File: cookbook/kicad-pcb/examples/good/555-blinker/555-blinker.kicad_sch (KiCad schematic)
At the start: 8 parts, among them J1 Conn_01x02, U1 NE555

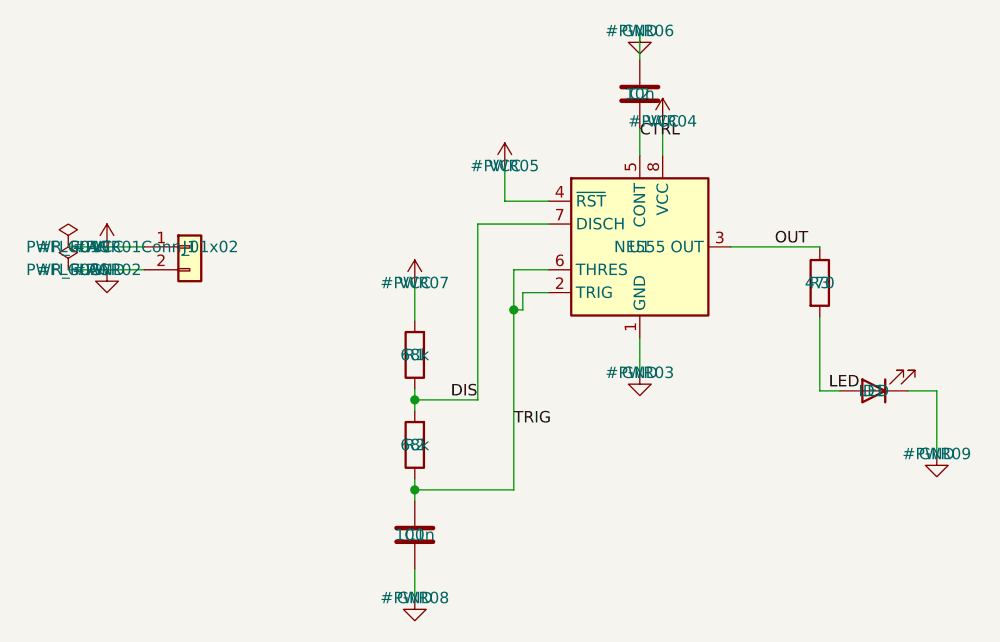
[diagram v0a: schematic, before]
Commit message: fix(cookbook/kicad-pcb): place schematic on 50-mil grid
The generator emitted pins and wire ends at arbitrary mm positions, so
ERC reported 51 endpoint_off_grid warnings. Move all coordinates to
integer 50-mil grid units (1.27 mm); symbol pin offsets are already
exact grid multiples so every endpoint lands on grid. ERC warnings drop
from 70 to 19 (all lib_symbol_issues, inherent to embedded symbols).
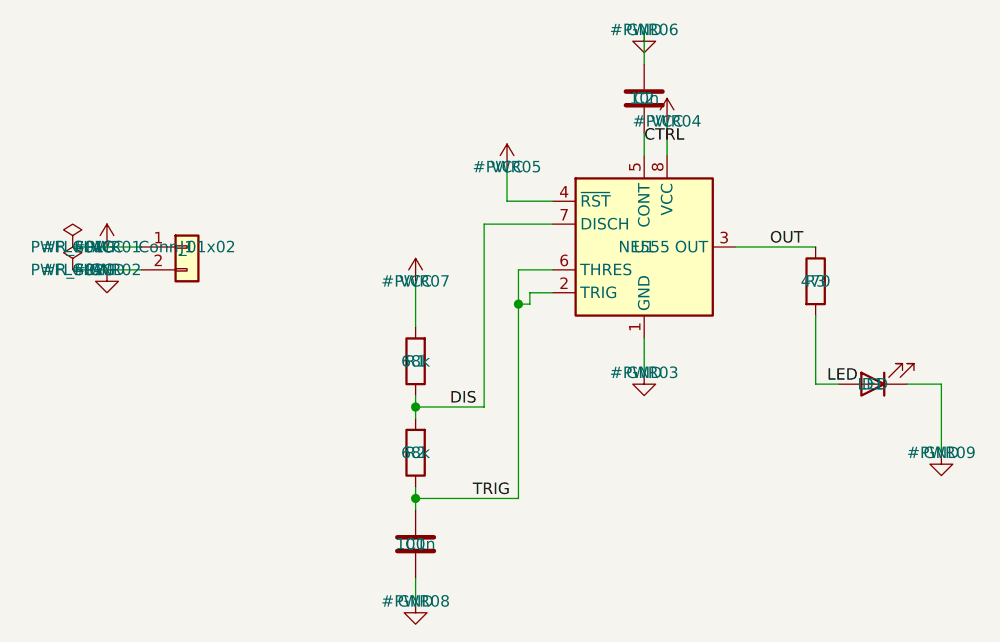
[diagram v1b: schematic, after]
